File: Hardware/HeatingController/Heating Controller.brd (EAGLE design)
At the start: 96.5 x 91.1 mm, 37 parts, among them IC1 ATMega 328p-pu, IC2 ULN2003AD, K1 G5LE, K2 G5LE, Q1 16MHz, X1 SWITCHED_OUT, X2 MAINS IN, X3 NEUTRAL

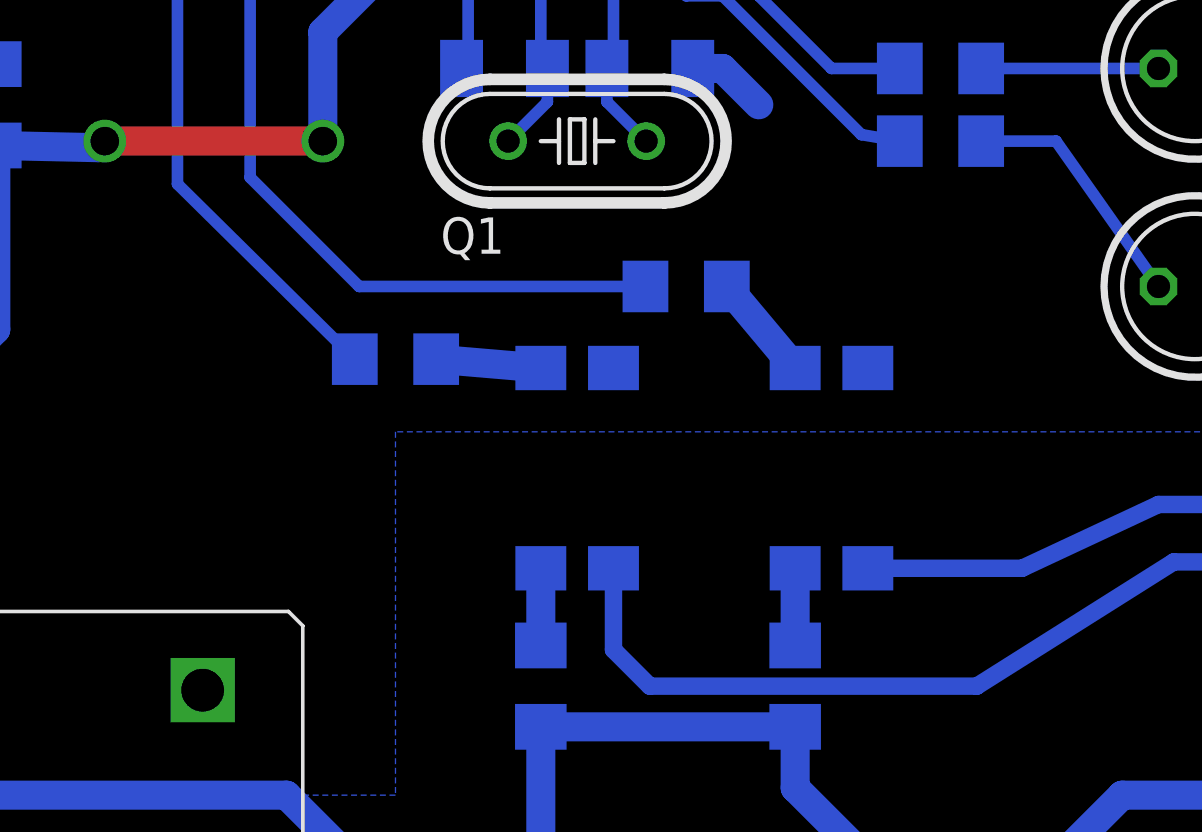
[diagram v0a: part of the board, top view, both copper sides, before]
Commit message: fixed incorrect optocoupler
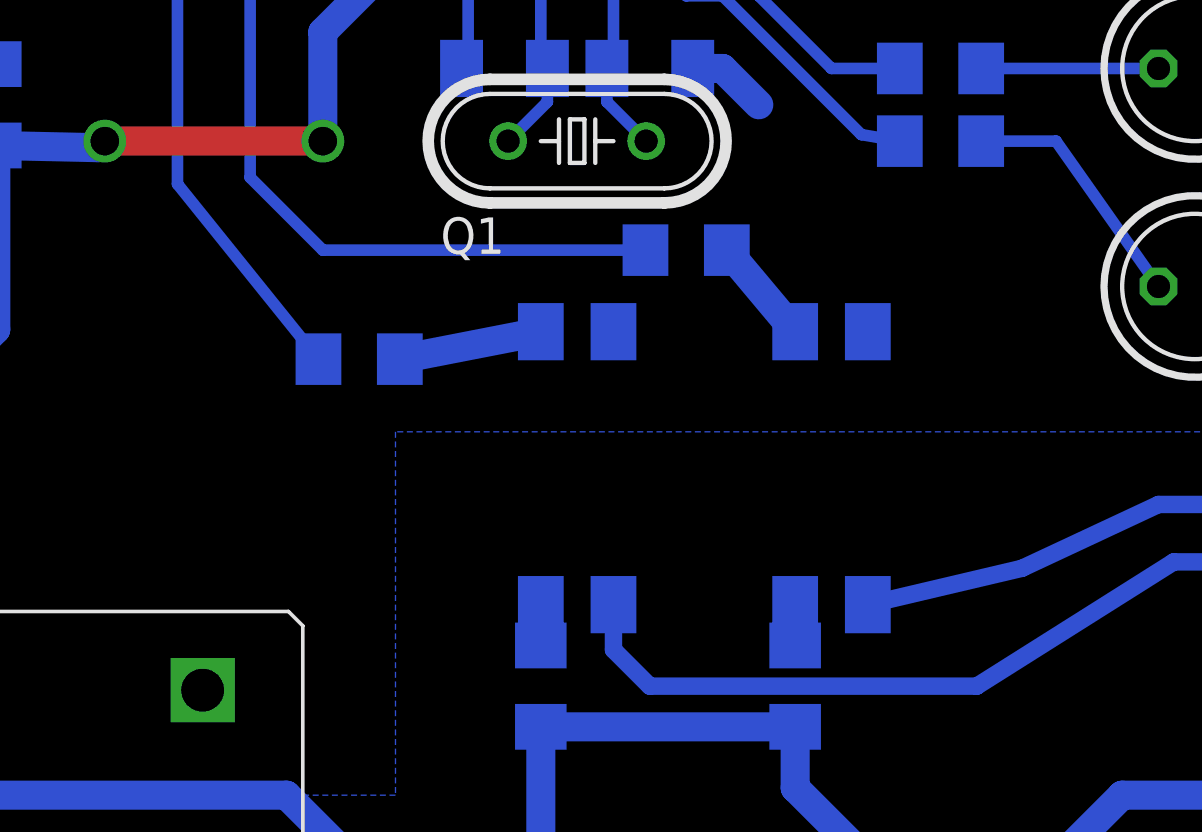
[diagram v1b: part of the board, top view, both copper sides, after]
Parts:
- OK1, OK2: device optocoupler:SMD4 -> optocoupler:DIL4-SMD
- moved R5 1.27 mm to (36.8, 53.3)
- moved R6 1.27 mm to (48.3, 57.1)
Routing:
- net N$11: track 3.67 -> 5.02 mm
- net N$22: track 30.7 -> 29.4 mm
- net N$21: track 2.70 -> 1.43 mm
- net N$20: track 2.70 -> 1.43 mm
- net HOTWATER_R: track 16.6 -> 15.7 mm
- net HEATING_R: track 23.0 -> 22.5 mm
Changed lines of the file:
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@@
 <element name="H3" library="holes" package="2,8" value="MOUNT-HOLE2.8" x="92.71" y="45.72"/>
 <element name="H4" library="holes" package="2,8" value="MOUNT-HOLE2.8" x="92.71" y="86.36"/>
-<element name="OK1" library="optocoupler" package="SMD4" value="LTV816S" x="44.45" y="49.53" smashed="yes" rot="MR180">
-<attribute name="OC_NEWARK" value="unknown" x="44.45" y="49.53" size="1.778" layer="28" rot="MR180" display="off"/>
-<attribute name="MPN" value="" x="44.45" y="49.53" size="1.778" layer="28" rot="MR180" display="off"/>
-<attribute name="MF" value="" x="44.45" y="49.53" size="1.778" layer="28" rot="MR180" display="off"/>
-<attribute name="OC_FARNELL" value="unknown" x="44.45" y="49.53" size="1.778" layer="28" rot="MR180" display="off"/>
+<element name="OK1" library="optocoupler" package="DIL4-SMD" value="LTV816S" x="44.45" y="49.53" smashed="yes" rot="MR180">
 <attribute name="NAME" x="41.91" y="50.165" size="1.27" layer="26" ratio="10" rot="MR270"/>
 <attribute name="VALUE" x="48.26" y="52.705" size="1.27" layer="28" ratio="10" rot="MR270"/>
 </element>
-<element name="OK2" library="optocoupler" package="SMD4" value="LTV816S" x="53.34" y="49.53" smashed="yes" rot="MR180">
-<attribute name="OC_NEWARK" value="unknown" x="53.34" y="49.53" size="1.778" layer="28" rot="MR180" display="off"/>
-<attribute name="MPN" value="" x="53.34" y="49.53" size="1.778" layer="28" rot="MR180" display="off"/>
-<attribute name="MF" value="" x="53.34" y="49.53" size="1.778" layer="28" rot="MR180" display="off"/>
-<attribute name="OC_FARNELL" value="unknown" x="53.34" y="49.53" size="1.778" layer="28" rot="MR180" display="off"/>
+<element name="OK2" library="optocoupler" package="DIL4-SMD" value="LTV816S" x="53.34" y="49.53" smashed="yes" rot="MR180">
 <attribute name="NAME" x="50.8" y="50.165" size="1.27" layer="26" ratio="10" rot="MR270"/>
 <attribute name="VALUE" x="57.15" y="52.705" size="1.27" layer="28" ratio="10" rot="MR270"/>
 </element>
-<element name="R5" library="rcl" package="R1206" value="" x="38.1" y="53.34" rot="MR0"/>
-<element name="R6" library="rcl" package="R1206" value="" x="48.26" y="55.88" smashed="yes" rot="MR0">
-<attribute name="NAME" x="53.34" y="55.88" size="1.27" layer="26" rot="MR0"/>
-<attribute name="VALUE" x="49.53" y="53.34" size="1.27" layer="28" rot="MR0"/>
+<element name="R5" library="rcl" package="R1206" value="" x="36.83" y="53.34" rot="MR0"/>
+<element name="R6" library="rcl" package="R1206" value="" x="48.26" y="57.15" smashed="yes" rot="MR0">
+<attribute name="NAME" x="53.34" y="57.15" size="1.27" layer="26" rot="MR0"/>
+<attribute name="VALUE" x="49.53" y="54.61" size="1.27" layer="28" rot="MR0"/>
 </element>
 <element name="R7" library="rcl" package="R1206" value="" x="43.18" y="41.91" rot="MR90"/>
@@
 <contactref element="R5" pad="2"/>
 <wire x1="30.48" y1="67.31" x2="30.48" y2="59.461" width="0.4064" layer="16"/>
-<wire x1="30.48" y1="59.461" x2="36.678" y2="53.34" width="0.4064" layer="16"/>
+<wire x1="30.48" y1="59.461" x2="35.408" y2="53.34" width="0.4064" layer="16"/>
 </signal>
 <signal name="HEATING_R">
@@
 <contactref element="R6" pad="2"/>
 <wire x1="33.02" y1="67.31" x2="33.02" y2="59.69" width="0.4064" layer="16"/>
-<wire x1="33.02" y1="59.69" x2="36.83" y2="55.88" width="0.4064" layer="16"/>
-<wire x1="36.83" y1="55.88" x2="46.838" y2="55.88" width="0.4064" layer="16"/>
+<wire x1="33.02" y1="59.69" x2="35.56" y2="57.15" width="0.4064" layer="16"/>
+<wire x1="35.56" y1="57.15" x2="46.838" y2="57.15" width="0.4064" layer="16"/>
 </signal>
 <signal name="N$9">
@@
 <contactref element="OK1" pad="1"/>
 <contactref element="R5" pad="1"/>
-<wire x1="43.18" y1="53.03" x2="39.522" y2="53.34" width="1.016" layer="16"/>
+<wire x1="43.18" y1="54.3" x2="38.252" y2="53.34" width="1.016" layer="16"/>
 </signal>
 <signal name="N$14">
 <contactref element="OK2" pad="1"/>
 <contactref element="R6" pad="1"/>
-<wire x1="49.682" y1="55.88" x2="52.07" y2="53.03" width="1.016" layer="16"/>
+<wire x1="49.682" y1="57.15" x2="52.07" y2="54.3" width="1.016" layer="16"/>
 </signal>
 <signal name="N$20">
 <contactref element="OK1" pad="4"/>
 <contactref element="R7" pad="2"/>
-<wire x1="43.18" y1="46.03" x2="43.18" y2="43.332" width="1.016" layer="16"/>
+<wire x1="43.18" y1="44.76" x2="43.18" y2="43.332" width="1.016" layer="16"/>
 </signal>
 <signal name="N$21">
 <contactref element="OK2" pad="4"/>
 <contactref element="R8" pad="2"/>
-<wire x1="52.07" y1="46.03" x2="52.07" y2="43.332" width="1.016" layer="16"/>
+<wire x1="52.07" y1="44.76" x2="52.07" y2="43.332" width="1.016" layer="16"/>
 </signal>
 <signal name="N$22">
@@
 <wire x1="71.755" y1="46.2534" x2="70.485" y2="46.2534" width="0.6096" layer="16"/>
 <wire x1="70.485" y1="46.2534" x2="65.3034" y2="46.2534" width="0.6096" layer="16"/>
-<wire x1="45.72" y1="46.03" x2="45.72" y2="43.18" width="0.6096" layer="16"/>
+<wire x1="45.72" y1="44.76" x2="45.72" y2="43.18" width="0.6096" layer="16"/>
 <wire x1="45.72" y1="43.18" x2="46.99" y2="41.91" width="0.6096" layer="16"/>
 <wire x1="46.99" y1="41.91" x2="58.42" y2="41.91" width="0.6096" layer="16"/>
@@
 <wire x1="73.025" y1="47.625" x2="72.39" y2="48.26" width="0.6096" layer="16"/>
 <wire x1="72.39" y1="48.26" x2="64.77" y2="48.26" width="0.6096" layer="16"/>
-<wire x1="54.61" y1="46.03" x2="60" y2="46.03" width="0.6096" layer="16"/>
+<wire x1="54.61" y1="44.76" x2="60" y2="46.03" width="0.6096" layer="16"/>
 <wire x1="60" y1="46.03" x2="64.77" y2="48.26" width="0.6096" layer="16"/>
 </signal>

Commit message: updated BOM with finalised pricelist
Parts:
- C5: value 1n -> 0.1u
- R3, R4: value 330R -> 3k3
- R5, R6, R7, R8: value (none) -> 120R
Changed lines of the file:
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@@
 </element>
 <element name="R2" library="rcl" package="R1206" value="10k" x="24.13" y="62.23" rot="MR270"/>
-<element name="R3" library="rcl" package="R1206" value="330R" x="57.15" y="63.5" rot="MR0"/>
-<element name="R4" library="rcl" package="R1206" value="330R" x="57.15" y="60.96" smashed="yes" rot="MR0">
+<element name="R3" library="rcl" package="R1206" value="3k3" x="57.15" y="63.5" rot="MR0"/>
+<element name="R4" library="rcl" package="R1206" value="3k3" x="57.15" y="60.96" smashed="yes" rot="MR0">
 <attribute name="NAME" x="58.42" y="58.42" size="1.27" layer="26" rot="MR0"/>
 <attribute name="VALUE" x="58.42" y="58.42" size="1.27" layer="28" rot="MR0"/>
@@
 <attribute name="VALUE" x="45.39" y="65.6" size="1.016" layer="28" rot="MR180"/>
 </element>
-<element name="C5" library="rcl" package="C1206K" value="1n" x="19.05" y="50.8" rot="MR90"/>
+<element name="C5" library="rcl" package="C1206K" value="0.1u" x="19.05" y="50.8" rot="MR90"/>
 <element name="IC2" library="uln-udn" package="SO16" value="ULN2003AD" x="74.93" y="43.18" rot="MR180"/>
 <element name="X1" library="con-wago-508" package="W237-4P" value="SWITCHED_OUT" x="71.12" y="6.35" smashed="yes">
@@
 <attribute name="VALUE" x="57.15" y="52.705" size="1.27" layer="28" ratio="10" rot="MR270"/>
 </element>
-<element name="R5" library="rcl" package="R1206" value="" x="36.83" y="53.34" rot="MR0"/>
-<element name="R6" library="rcl" package="R1206" value="" x="48.26" y="57.15" smashed="yes" rot="MR0">
+<element name="R5" library="rcl" package="R1206" value="120R" x="36.83" y="53.34" rot="MR0"/>
+<element name="R6" library="rcl" package="R1206" value="120R" x="48.26" y="57.15" smashed="yes" rot="MR0">
 <attribute name="NAME" x="53.34" y="57.15" size="1.27" layer="26" rot="MR0"/>
 <attribute name="VALUE" x="49.53" y="54.61" size="1.27" layer="28" rot="MR0"/>
 </element>
-<element name="R7" library="rcl" package="R1206" value="" x="43.18" y="41.91" rot="MR90"/>
-<element name="R8" library="rcl" package="R1206" value="" x="52.07" y="41.91" rot="MR90"/>
+<element name="R7" library="rcl" package="R1206" value="120R" x="43.18" y="41.91" rot="MR90"/>
+<element name="R8" library="rcl" package="R1206" value="120R" x="52.07" y="41.91" rot="MR90"/>
 <element name="L1" library="rcl" package="L3230M" value="" x="7.62" y="45.72" rot="MR90"/>
 <element name="L2" library="rcl" package="L3230M" value="" x="40.64" y="34.29" rot="MR180"/>
